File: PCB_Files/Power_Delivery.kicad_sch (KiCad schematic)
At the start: 15 parts, among them SW2 SW_SPST, U4 SPX1117M3-L-3-3/TR

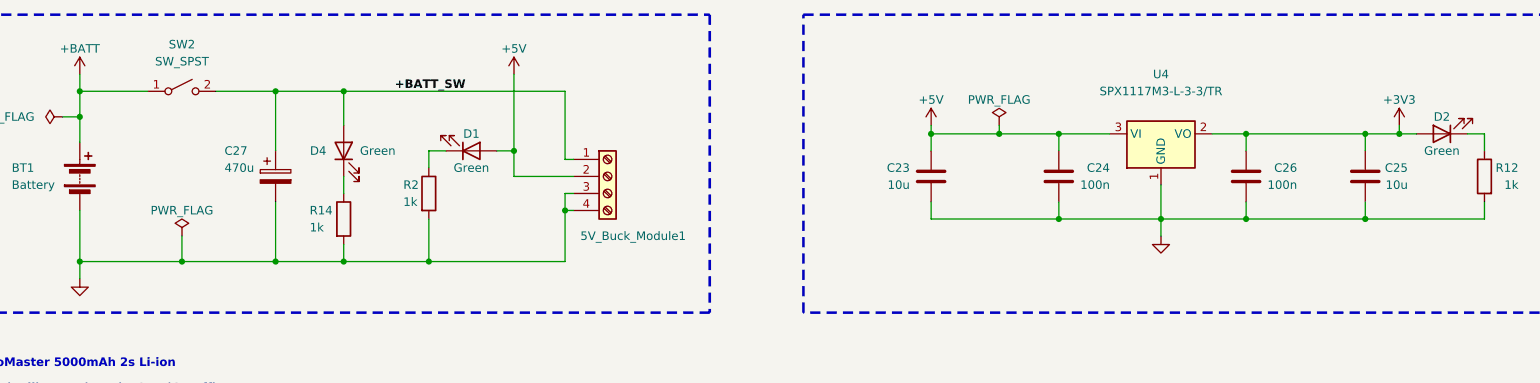
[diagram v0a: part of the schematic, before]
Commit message: Cleaned up Bi-directional LED indicator schematic layout for motor controllers.
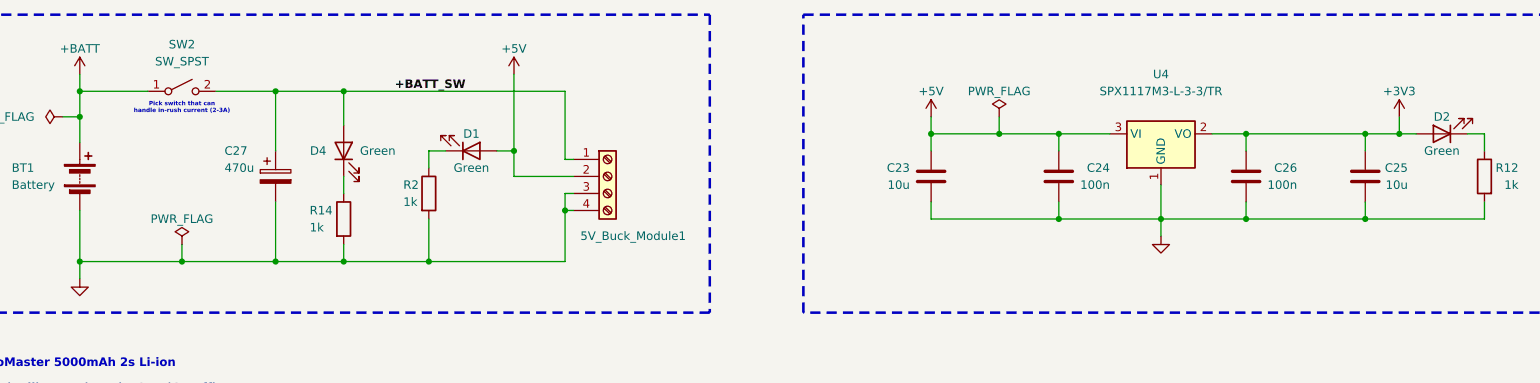
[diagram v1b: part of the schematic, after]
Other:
- note added: "Pick switch that can handle in-rush current (2-3A)"
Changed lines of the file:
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@@
+		)
+	)
+	(text "Pick switch that can \nhandle in-rush current (2-3A)"
+		(exclude_from_sim no)
+		(at 50.8 43.18 0)
+		(effects
+			(font
+				(size 0.635 0.635)
+				(thickness 0.254)
+				(bold yes)
+				(color 0 0 0 1)
+			)
 		)
 	)
@@
 	)
 	(junction
+		(at 232.41 46.99)
+		(diameter 0)
+		(color 0 0 0 0)
+	)
+	(junction
 		(at 74.93 40.64)
 		(diameter 0)
@@
 	)
 	(junction
-		(at 172.72 46.99)
+		(at 74.93 66.04)
 		(diameter 0)
 		(color 0 0 0 0)
 	)
 	(junction
-		(at 74.93 66.04)
+		(at 209.55 46.99)
+		(diameter 0)
+		(color 0 0 0 0)
+	)
+	(junction
+		(at 64.77 66.04)
+		(diameter 0)
+		(color 0 0 0 0)
+	)
+	(junction
+		(at 196.85 59.69)
+		(diameter 0)
+		(color 0 0 0 0)
+	)
+	(junction
+		(at 50.8 66.04)
+		(diameter 0)
+		(color 0 0 0 0)
+	)
+	(junction
+		(at 181.61 59.69)
+		(diameter 0)
+		(color 0 0 0 0)
+	)
+	(junction
+		(at 35.56 40.64)
+		(diameter 0)
+		(color 0 0 0 0)
+	)
+	(junction
+		(at 172.72 46.99)
 		(diameter 0)
 		(color 0 0 0 0)
@@
 	)
 	(junction
-		(at 209.55 46.99)
-		(diameter 0)
-		(color 0 0 0 0)
-	)
-	(junction
-		(at 64.77 66.04)
-		(diameter 0)
-		(color 0 0 0 0)
-	)
-	(junction
-		(at 196.85 59.69)
-		(diameter 0)
-		(color 0 0 0 0)
-	)
-	(junction
-		(at 50.8 66.04)
-		(diameter 0)
-		(color 0 0 0 0)
-	)
-	(junction
-		(at 181.61 59.69)
-		(diameter 0)
-		(color 0 0 0 0)
-	)
-	(junction
-		(at 35.56 40.64)
-		(diameter 0)
-		(color 0 0 0 0)
-	)
-	(junction
 		(at 35.56 44.45)
 		(diameter 0)
 		(color 0 0 0 0)
 	)
-	(junction
-		(at 232.41 46.99)
-		(diameter 0)
-		(color 0 0 0 0)
-	)
 	(wire
 		(pts
@@
 	(wire
 		(pts
-			(xy 172.72 45.72) (xy 172.72 46.99)
+			(xy 172.72 44.45) (xy 172.72 46.99)
 		)
 		(stroke
@@
 	(wire
 		(pts
-			(xy 50.8 62.23) (xy 50.8 66.04)
+			(xy 50.8 63.5) (xy 50.8 66.04)
 		)
 		(stroke
@@
 	(wire
 		(pts
-			(xy 232.41 45.72) (xy 232.41 46.99)
+			(xy 232.41 44.45) (xy 232.41 46.99)
 		)
 		(stroke
@@
 	(wire
 		(pts
-			(xy 162.56 45.72) (xy 162.56 46.99)
+			(xy 162.56 44.45) (xy 162.56 46.99)
 		)
 		(stroke
@@
 	(symbol
 		(lib_id "power:+5V")
-		(at 162.56 45.72 0)
+		(at 162.56 44.45 0)
 		(unit 1)
 		(body_style 1)
@@
 		(dnp no)
 		(property "Reference" "#PWR047"
-			(at 162.56 49.53 0)
+			(at 162.56 48.26 0)
 			(hide yes)
 			(show_name no)
@@
 		)
 		(property "Value" "+5V"
-			(at 162.56 41.91 0)
+			(at 162.56 40.64 0)
 			(show_name no)
 			(do_not_autoplace no)
@@
 		)
 		(property "Footprint" ""
-			(at 162.56 45.72 0)
+			(at 162.56 44.45 0)
 			(hide yes)
 			(show_name no)
@@
 		)
 		(property "Datasheet" ""
-			(at 162.56 45.72 0)
+			(at 162.56 44.45 0)
 			(hide yes)
 			(show_name no)
@@
 		)
 		(property "Description" "Power symbol creates a global label with name \"+5V\""
-			(at 162.56 45.72 0)
+			(at 162.56 44.45 0)
 			(hide yes)
 			(show_name no)
@@
 	(symbol
 		(lib_id "power:+3.3V")
-		(at 232.41 45.72 0)
+		(at 232.41 44.45 0)
 		(unit 1)
 		(body_style 1)
@@
 		(dnp no)
 		(property "Reference" "#PWR035"
-			(at 232.41 49.53 0)
+			(at 232.41 48.26 0)
 			(hide yes)
 			(show_name no)
@@
 		)
 		(property "Value" "+3V3"
-			(at 232.41 41.91 0)
+			(at 232.41 40.64 0)
 			(show_name no)
 			(do_not_autoplace no)
@@
 		)
 		(property "Footprint" ""
-			(at 232.41 45.72 0)
+			(at 232.41 44.45 0)
 			(hide yes)
 			(show_name no)
@@
 		)
 		(property "Datasheet" ""
-			(at 232.41 45.72 0)
+			(at 232.41 44.45 0)
 			(hide yes)
 			(show_name no)
@@
 		)
 		(property "Description" "Power symbol creates a global label with name \"+3.3V\""
-			(at 232.41 45.72 0)
+			(at 232.41 44.45 0)
 			(hide yes)
 			(show_name no)
@@
 	(symbol
 		(lib_id "power:PWR_FLAG")
-		(at 50.8 62.23 0)
+		(at 50.8 63.5 0)
 		(unit 1)
 		(body_style 1)
@@
 		(dnp no)
 		(property "Reference" "#FLG04"
-			(at 50.8 60.325 0)
+			(at 50.8 61.595 0)
 			(hide yes)
 			(show_name no)
@@
 		)
 		(property "Value" "PWR_FLAG"
-			(at 50.8 58.42 0)
+			(at 50.8 59.69 0)
 			(show_name no)
 			(do_not_autoplace no)
@@
 		)
 		(property "Footprint" ""
-			(at 50.8 62.23 0)
+			(at 50.8 63.5 0)
 			(hide yes)
 			(show_name no)
@@
 		)
 		(property "Datasheet" ""
-			(at 50.8 62.23 0)
+			(at 50.8 63.5 0)
 			(hide yes)
 			(show_name no)
@@
 		)
 		(property "Description" "Special symbol for telling ERC where power comes from"
-			(at 50.8 62.23 0)
+			(at 50.8 63.5 0)
 			(hide yes)
 			(show_name no)
@@
 	(symbol
 		(lib_id "power:PWR_FLAG")
-		(at 172.72 45.72 0)
+		(at 172.72 44.45 0)
 		(unit 1)
 		(body_style 1)
@@
 		(dnp no)
 		(property "Reference" "#FLG02"
-			(at 172.72 43.815 0)
+			(at 172.72 42.545 0)
 			(hide yes)
 			(show_name no)
@@
 		)
 		(property "Value" "PWR_FLAG"
-			(at 172.72 41.91 0)
+			(at 172.72 40.64 0)
 			(show_name no)
 			(do_not_autoplace no)
@@
 		)
 		(property "Footprint" ""
-			(at 172.72 45.72 0)
+			(at 172.72 44.45 0)
 			(hide yes)
 			(show_name no)
@@
 		)
 		(property "Datasheet" ""
-			(at 172.72 45.72 0)
+			(at 172.72 44.45 0)
 			(hide yes)
 			(show_name no)
@@
 		)
 		(property "Description" "Special symbol for telling ERC where power comes from"
-			(at 172.72 45.72 0)
-			(hide yes)
-			(show_name no)
+			(at 172.72 44.45 0)
+			(hide yes)
+			(show_name no)

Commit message: Changed +BATT net name to +VBAT, +BATT_SW to +VBAT_SW, and now motor controllers are powered by net name +VBAT_SW. This clearly seperates +VBAT before the switch, +VBAT_SW after the switch, +5V, and +3V3 / +3V3A.
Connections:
- net GND: no longer 5V_Buck_Module1.3 (Pin_3), 5V_Buck_Module1.4 (Pin_4), BT1.2 (-), C27.2, R14.2, R2.2
- net +BATT renamed +VBAT
- net +BATT_SW renamed +VBAT_SW
- new net GNDPWR: 5V_Buck_Module1.3 (Pin_3), 5V_Buck_Module1.4 (Pin_4), BT1.2 (-), C27.2, R14.2, R2.2
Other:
- note added: "5V from Buck Converter Module into LDO Regulator to 3V3"
- note added: "8V4/6V4 into Buck Converter Module to 5V"

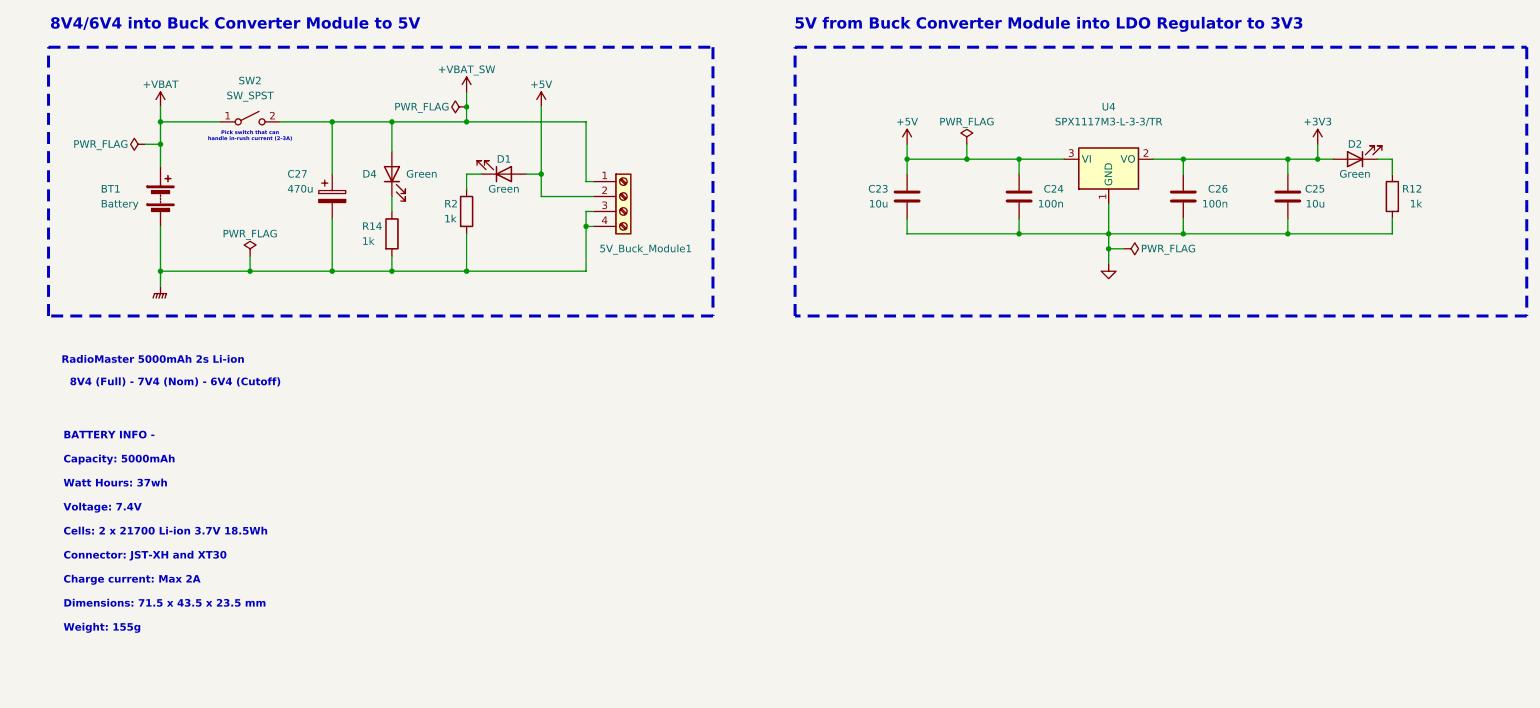
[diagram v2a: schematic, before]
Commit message: Added IC buck converter symbol and footprint to schematic. Will create own buck converter design on board.
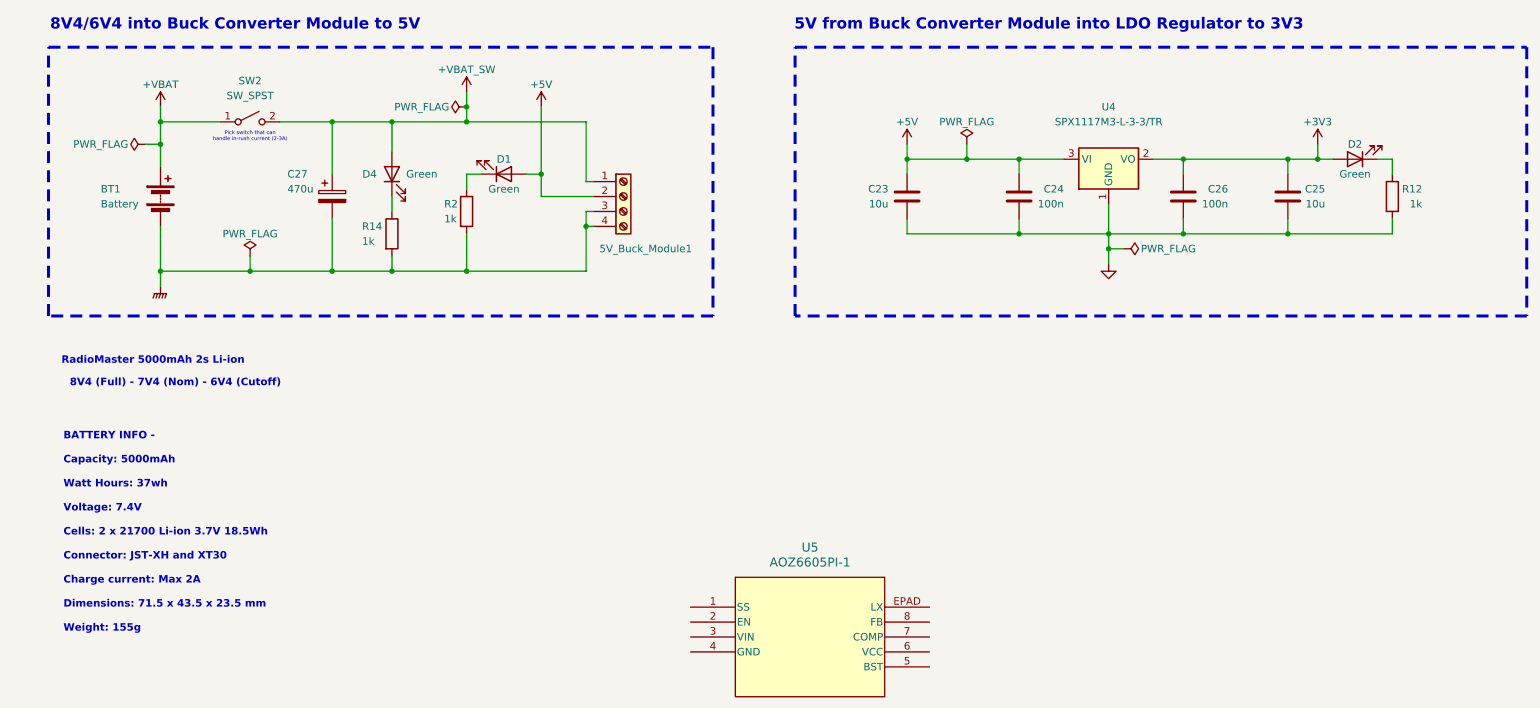
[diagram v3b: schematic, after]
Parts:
- added U5: AOZ6605PI-1, SO8_EP1_AOS, symbol SO8_EP1_AOS:AOZ6605PI-1
- C23, C25: footprint Capacitor_SMD:C_0603_1608Metric -> Capacitor_SMD:C_0805_2012Metric
- C27: footprint (none) -> Capacitor_SMD:C_0805_2012Metric
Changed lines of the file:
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@@
-		)
-	)
-	(rectangle
-		(start 121.92 71.12)
-		(end 121.92 71.12)
-		(stroke
-			(width 0)
-			(type default)
-		)
-		(fill
-			(type none)
 		)
 	)
@@
 			(font
 				(size 0.635 0.635)
-				(thickness 0.254)
-				(bold yes)
+				(thickness 0.0794)
 				(color 0 0 0 1)
 			)
@@
 			(font
 				(size 1.905 1.905)
-				(thickness 0.254)
+				(thickness 0.381)
 				(bold yes)
 			)
@@
 			(font
 				(size 1.905 1.905)
-				(thickness 0.254)
+				(thickness 0.381)
 				(bold yes)
 			)
@@
 	)
 	(symbol
+		(lib_id "SO8_EP1_AOS:AOZ6605PI-1")
+		(at 146.05 128.27 0)
+		(unit 1)
+		(body_style 1)
+		(exclude_from_sim no)
+		(in_bom yes)
+		(on_board yes)
+		(in_pos_files yes)
+		(dnp no)
+		(fields_autoplaced yes)
+		(property "Reference" "U5"
+			(at 146.05 113.03 0)
+			(show_name no)
+			(do_not_autoplace no)
+			(effects
+				(font
+					(size 1.524 1.524)
+				)
+			)
+		)
+		(property "Value" "AOZ6605PI-1"
+			(at 146.05 115.57 0)
+			(show_name no)
+			(do_not_autoplace no)
+			(effects
+				(font
+					(size 1.524 1.524)
+				)
+			)
+		)
+		(property "Footprint" "SO8_EP1_AOS"
+			(at 125.73 123.19 0)
+			(hide yes)
+			(show_name no)
+			(do_not_autoplace no)
+			(effects
+				(font
+					(size 1.27 1.27)
+					(italic yes)
+				)
+			)
+		)
+		(property "Datasheet" "AOZ6605PI-1"
+			(at 125.73 123.19 0)
+			(hide yes)
+			(show_name no)
+			(do_not_autoplace no)
+			(effects
+				(font
+					(size 1.27 1.27)
+					(italic yes)
+				)
+			)
+		)
+		(property "Description" ""
+			(at 146.05 128.27 0)
+			(hide yes)
+			(show_name no)
+			(do_not_autoplace no)
+			(effects
+				(font
+					(size 1.27 1.27)
+				)
+			)
+		)
+		(pin "2"
+		)
+		(pin "6"
+		)
+		(pin "1"
+		)
+		(pin "EPAD"
+		)
+		(pin "8"
+		)
+		(pin "4"
+		)
+		(pin "7"
+		)
+		(pin "3"
+		)
+		(pin "5"
+		)
+		(instances
+			(project "Sensor_Integration_Board"
+				(path "/0eab3e03-be91-4947-b3db-b5c169582a4b/e3d20648-cf59-48a4-a1f4-1454d372f010"
+					(reference "U5")
+					(unit 1)
+				)
+			)
+		)
+	)
+	(symbol
 		(lib_id "Device:Battery")
 		(at 35.56 53.34 0)
@@
 			)
 		)
-		(property "Footprint" ""
+		(property "Footprint" "Capacitor_SMD:C_0805_2012Metric"
 			(at 65.7352 57.15 0)
 			(hide yes)
@@
 			)
 		)
-		(property "Footprint" "Capacitor_SMD:C_0603_1608Metric"
+		(property "Footprint" "Capacitor_SMD:C_0805_2012Metric"
 			(at 161.5948 57.15 0)
 			(hide yes)
@@
 			)
 		)
-		(property "Footprint" "Capacitor_SMD:C_0603_1608Metric"
+		(property "Footprint" "Capacitor_SMD:C_0805_2012Metric"
 			(at 226.3648 57.15 0)
 			(hide yes)
